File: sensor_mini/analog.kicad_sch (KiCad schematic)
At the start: 7 parts, among them J3 Thermistor_conn, J4 Tank_pressure_conn

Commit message: Clean Up
Removed old files
Cleaned up Schematics
Created new PDFs
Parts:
- renumbered J3 to J2, J4 to J3, R7 to R5, R8 to R6, R9 to R7
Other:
- note added: "Thermistor creates a voltage divider with R7. The resistance is measured using that voltage."
- note added: "Voltage from pin 2 is scaled down with resistor divider and measured."
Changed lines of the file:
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@@
     (stroke (width 0) (type default) (color 0 0 0 0))
+  )
+  (text "Thermistor creates a voltage divider with R7.\nThe resistance is measured using that voltage."
+    (at 171.45 72.39 0)
+    (effects (font (size 1.27 1.27)) (justify left bottom))
+  )
+  (text "Voltage from pin 2 is scaled down with\nresistor divider and measured."
+    (at 172.72 114.3 0)
+    (effects (font (size 1.27 1.27)) (justify left bottom))
   )
   (hierarchical_label "THERM_0" (shape input) (at 132.08 88.9 180)
@@
   (symbol (lib_id "sensors-rescue:Conn_01x03_Female-Connector") (at 165.1 124.46 0) (unit 1)
     (in_bom yes) (on_board yes)
-    (property "Reference" "J4" (id 0) (at 165.8112 123.7996 0)
+    (property "Reference" "J3" (id 0) (at 165.8112 123.7996 0)
       (effects (font (size 1.27 1.27)) (justify left))
     )
@@
     (pin "3")
   )
-  (symbol (lib_id "sensors-rescue:Conn_01x02_Female-Connector") (at 165.1 88.9 0)
+  (symbol (lib_id "sensors-rescue:Conn_01x02_Female-Connector") (at 165.1 88.9 0) (unit 1)
     (in_bom yes) (on_board yes)
-    (property "Reference" "J3" (id 0) (at 165.7858 89.5096 0)
+    (property "Reference" "J2" (id 0) (at 165.7858 89.5096 0)
       (effects (font (size 1.27 1.27)) (justify left))
     )
@@
   (symbol (lib_id "Device:R") (at 154.94 81.28 0) (unit 1)
     (in_bom yes) (on_board yes)
-    (property "Reference" "R9" (id 0) (at 156.718 80.1116 0)
+    (property "Reference" "R7" (id 0) (at 156.718 80.1116 0)
       (effects (font (size 1.27 1.27)) (justify left))
     )
@@
   (symbol (lib_id "power:+15V") (at 154.94 119.38 0) (unit 1)
     (in_bom yes) (on_board yes)
-    (property "Reference" "#PWR058" (id 0) (at 154.94 123.19 0)
+    (property "Reference" "#PWR039" (id 0) (at 154.94 123.19 0)
       (effects (font (size 1.27 1.27)) hide)
     )
@@
   (symbol (lib_id "power:GND") (at 154.94 129.54 0) (unit 1)
     (in_bom yes) (on_board yes)
-    (property "Reference" "#PWR059" (id 0) (at 154.94 135.89 0)
+    (property "Reference" "#PWR040" (id 0) (at 154.94 135.89 0)
       (effects (font (size 1.27 1.27)) hide)
     )
@@
   (symbol (lib_id "power:GND") (at 154.94 93.98 0) (unit 1)
     (in_bom yes) (on_board yes)
-    (property "Reference" "#PWR057" (id 0) (at 154.94 100.33 0)
+    (property "Reference" "#PWR038" (id 0) (at 154.94 100.33 0)
       (effects (font (size 1.27 1.27)) hide)
     )
@@
   (symbol (lib_id "Device:R") (at 142.24 128.27 0) (unit 1)
     (in_bom yes) (on_board yes)
-    (property "Reference" "R7" (id 0) (at 144.018 127.1016 0)
+    (property "Reference" "R5" (id 0) (at 144.018 127.1016 0)
       (effects (font (size 1.27 1.27)) (justify left))
     )
@@
   (symbol (lib_id "Device:R") (at 142.24 139.7 0) (unit 1)
     (in_bom yes) (on_board yes)
-    (property "Reference" "R8" (id 0) (at 144.018 138.5316 0)
+    (property "Reference" "R6" (id 0) (at 144.018 138.5316 0)
       (effects (font (size 1.27 1.27)) (justify left))
     )
@@
   (symbol (lib_id "power:GND") (at 142.24 143.51 0) (unit 1)
     (in_bom yes) (on_board yes)
-    (property "Reference" "#PWR055" (id 0) (at 142.24 149.86 0)
+    (property "Reference" "#PWR036" (id 0) (at 142.24 149.86 0)
       (effects (font (size 1.27 1.27)) hide)
     )
@@
     (pin "1")
   )
-  (symbol (lib_id "power:+3V3") (at 154.94 73.66 0)
+  (symbol (lib_id "power:+3V3") (at 154.94 73.66 0) (unit 1)
     (in_bom yes) (on_board yes)
-    (property "Reference" "#PWR056" (id 0) (at 154.94 77.47 0)
+    (property "Reference" "#PWR037" (id 0) (at 154.94 77.47 0)
       (effects (font (size 1.27 1.27)) hide)
     )

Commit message: ICM-20948
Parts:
- added J? (x3): Thermistor_conn, Connector_JST:JST_PH_S2B-PH-K_1x02_P2.00mm_Horizontal, symbol sensors-rescue:Conn_01x02_Female-Connector
- added R? (x6): R, symbol Device:R
- added R?: R, Resistor_SMD:R_0805_2012Metric_Pad1.15x1.40mm_HandSolder, symbol Device:R
- added TP?: TestPoint, TestPoint:TestPoint_THTPad_2.0x2.0mm_Drill1.0mm, symbol Connector:TestPoint
- added U?: TLV9002IDR, SOIC127P599X175-8N, symbol TLV9002IDR:TLV9002IDR
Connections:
- net +3V3: now also R?.1
- net GND: now also J?.2 (Pin_2), R?.1, R?.2, U?.4 (V-)
- net THERM_0: now also J?.1 (Pin_1), R?.2, TP?.1
- new net: R?.1, R?.1, R?.2, U?.2
- new net: R?.1, R?.1, R?.2, U?.6
- new net: R?.2, U?.7
- new net: J?.1 (Pin_1), U?.5
- new net: R?.2, U?.1
- new net: J?.2 (Pin_2), U?.3
- new net +3.3V: J?.1 (Pin_1), J?.2 (Pin_2), R?.1, R?.2, U?.8 (V+)
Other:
- note added: "Reference Application Note: https://www.ti.com/lit/an/sboa323a/sboa323a.pdf?ts=1668083218662&ref_url=https%253A%252F%252Fwww.google.com%252F"
- note added: "Wheat Stone Bridge Circuit #2"
- note added: "WheatStone Bridge Circuit #1"
- moved on the sheet: J2, J3, R5, R6, R7, TP5, TP6

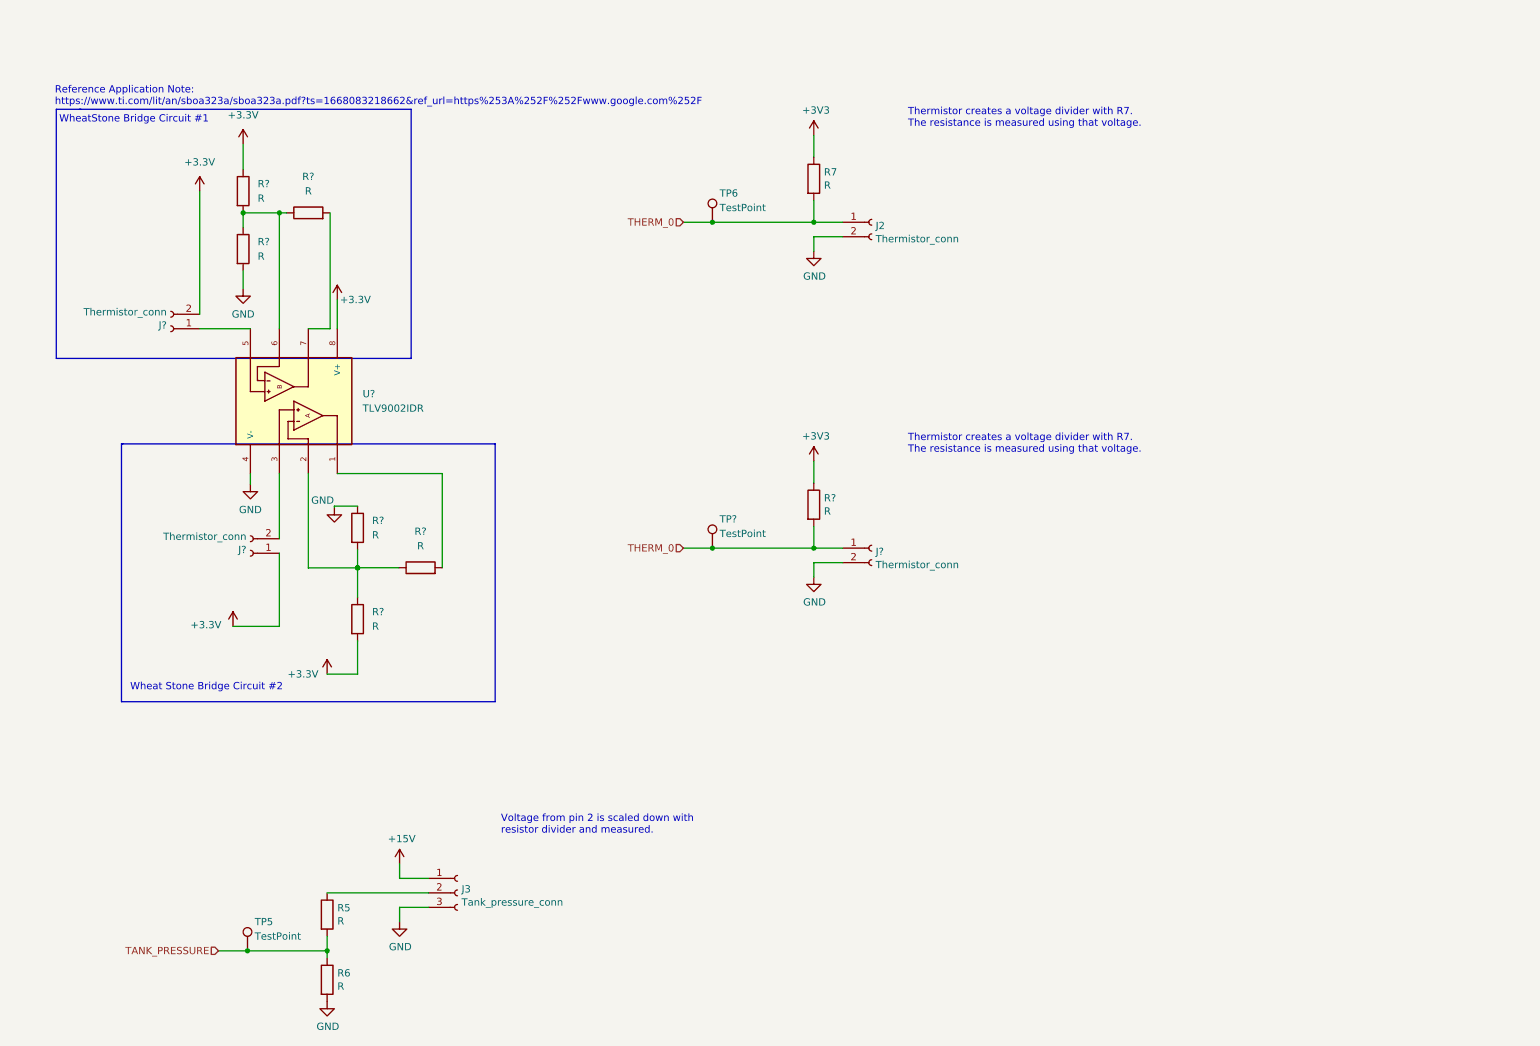
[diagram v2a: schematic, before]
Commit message: Finish Analog Sensors Schematic
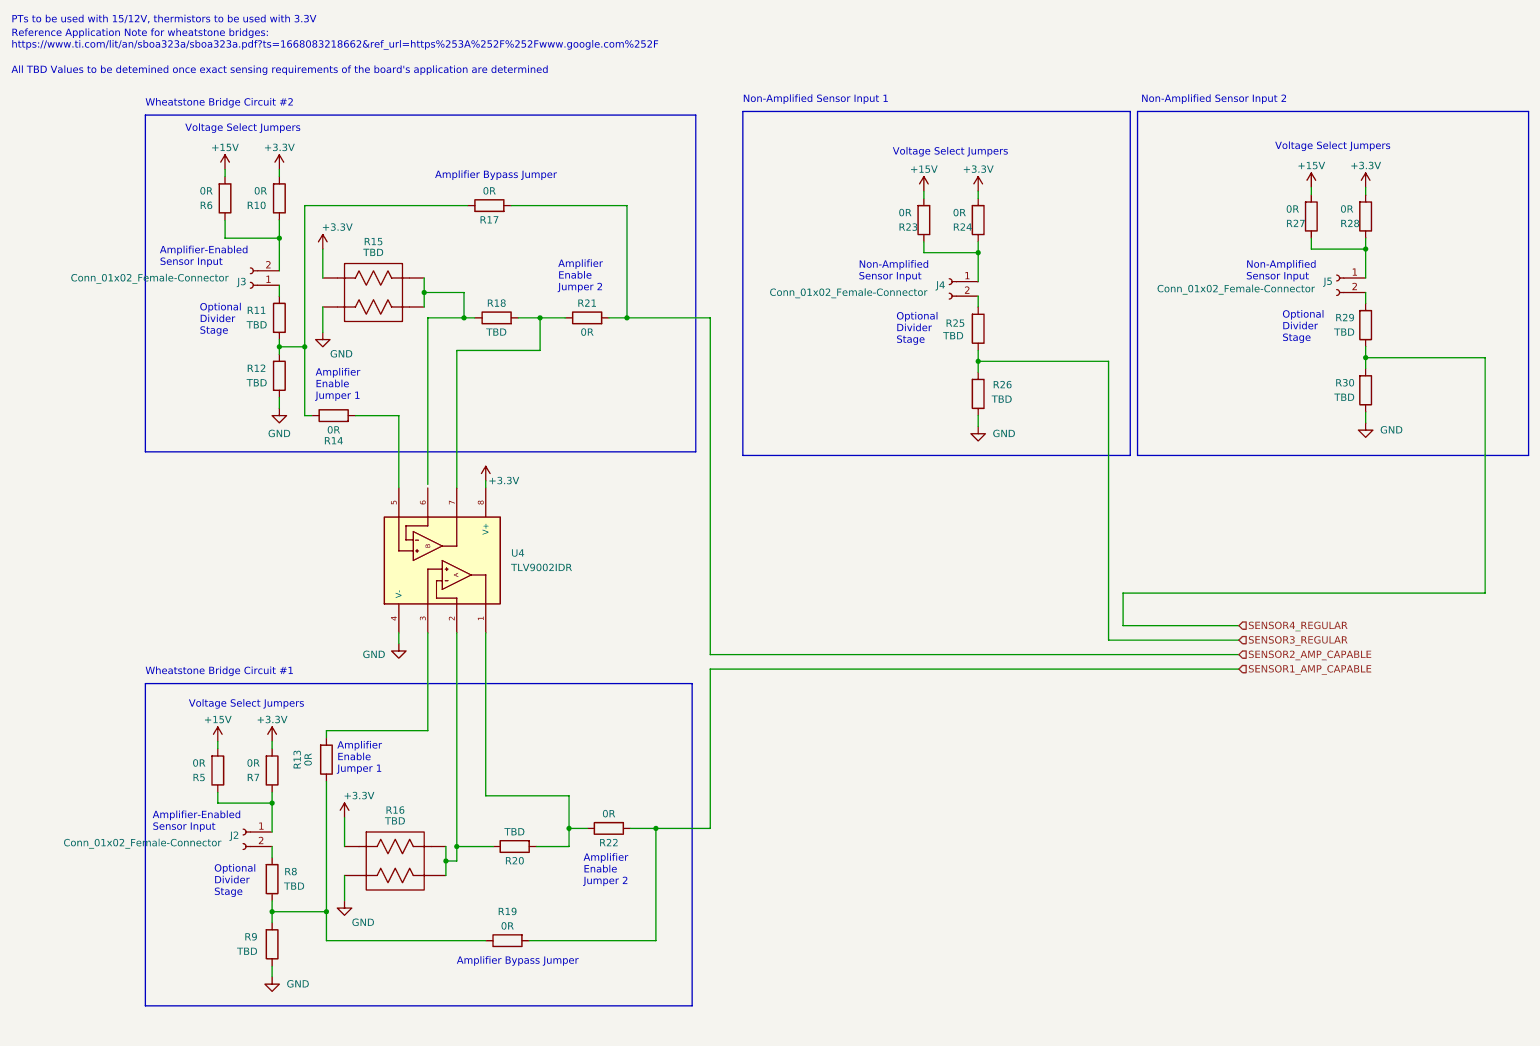
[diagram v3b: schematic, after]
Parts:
- removed J3: Tank_pressure_conn, Connector_JST:JST_PH_S3B-PH-K_1x03_P2.00mm_Horizontal, symbol sensors-rescue:Conn_01x03_Female-Connector
- removed J? (x2): Thermistor_conn, Connector_JST:JST_PH_S2B-PH-K_1x02_P2.00mm_Horizontal, symbol sensors-rescue:Conn_01x02_Female-Connector
- removed R? (x5): R, symbol Device:R
- removed R?: R, Resistor_SMD:R_0805_2012Metric_Pad1.15x1.40mm_HandSolder, symbol Device:R
- removed TP5, TP6, TP?: TestPoint, TestPoint:TestPoint_THTPad_2.0x2.0mm_Drill1.0mm, symbol Connector:TestPoint
- added J4, J5: Conn_01x02_Female-Connector, Connector_JST:JST_PH_S2B-PH-K_1x02_P2.00mm_Horizontal, symbol sensors-rescue:Conn_01x02_Female-Connector
- added R10, R13, R14, R17, R19, R21, R22, R23, R24, R27, R28: 0R, symbol Device:R
- added R11, R12, R20, R25, R26, R29, R30, R8, R9: TBD, symbol Device:R
- added R15, R16: TBD, symbol ACA_Percision_Vishay:2_RES_ARRAY
- J2: value Thermistor_conn -> Conn_01x02_Female-Connector
- J3: renamed from J?; value Thermistor_conn -> Conn_01x02_Female-Connector
- R18: renamed from R?; value R -> TBD
- R5, R6, R7: value R -> 0R; footprint Resistor_SMD:R_0805_2012Metric_Pad1.15x1.40mm_HandSolder -> (none)
- gave numbers to parts that had none: 1
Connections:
- net +15V: now also R5.2, R6.2, R23.2, R27.2
- net +3V3: now also R7.2, U4.8 (V+), R10.2, R15., R16., R24.2, R28.2; no longer R7.1
- net GND: now also R12.2, R15., R16., R26.1, R30.1, R9.1; no longer J2.2 (Pin_2), R6.2
- net at R5.1: now also J2.1 (Pin_1), R7.1
- net at U4.2: now also R16., R20.1
- net at R18.1: now also R15.; no longer U4.6
- net at R18.2, U4.7: now also R21.1
- net at J3.1 (Pin_1): now also R11.1; no longer U4.5
- net at U4.1: now also R20.2, R22.1
- net at U4.3: now also R13.2
- net +3.3V: no longer names the net of J3.2 (Pin_2)
- net +3.3V: now also R6.1, R10.1; no longer U4.8 (V+)
- removed net TANK_PRESSURE: R5.2, R6.1
- removed net THERM_0: J2.1 (Pin_1), R7.2
- new net: J5.1 (Pin_1), R27.1, R28.1
- new net: J5.2 (Pin_2), R29.2
- new net: R13.1, R19.1, R8.1, R9.2
- new net: J4.1 (Pin_1), R23.1, R24.1
- new net: J4.2 (Pin_2), R25.2
- new net: R11.2, R12.1, R14.1, R17.1
- new net: R14.2, U4.5
- new net: J2.2 (Pin_2), R8.2
- new net SENSOR1_AMP_CAPABLE: R19.2, R22.2
- new net SENSOR2_AMP_CAPABLE: R17.2, R21.2
- new net SENSOR3_REGULAR: R25.1, R26.2
- new net SENSOR4_REGULAR: R29.1, R30.2
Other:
- note added: "All TBD Values to be detemined once exact sensing requirements of the board's application are determined"
- note added: "Amplifier Bypass Jumper"
- note added: "Amplifier Enable Jumper 1"
- note added: "Amplifier Enable Jumper 2"
- note added: "Amplifier-Enabled Sensor Input"
- note added: "Non-Amplified Sensor Input"
- note added: "Non-Amplified Sensor Input 1"
- note added: "Non-Amplified Sensor Input 2"
- note added: "Optional Divider Stage"
- note added: "PTs to be used with 15/12V, thermistors to be used with 3.3V"
- note added: "Reference Application Note for wheatstone bridges: https://www.ti.com/lit/an/sboa323a/sboa323a.pdf?ts=1668083218662&ref_url=https%253A%252F%252Fwww.google.com%252F"
- note added: "Voltage Select Jumpers"
- note added: "Wheatstone Bridge Circuit #1"
- note added: "Wheatstone Bridge Circuit #2"
- note removed: "Reference Application Note: https://www.ti.com/lit/an/sboa323a/sboa323a.pdf?ts=1668083218662&ref_url=https%253A%252F%252Fwww.google.com%252F"
- note removed: "Thermistor creates a voltage divider with R7. The resistance is measured using that voltage."
- note removed: "Voltage from pin 2 is scaled down with resistor divider and measured."
- note removed: "Wheat Stone Bridge Circuit #2"
- note removed: "WheatStone Bridge Circuit #1"
- moved on the sheet: J3, R18, U4

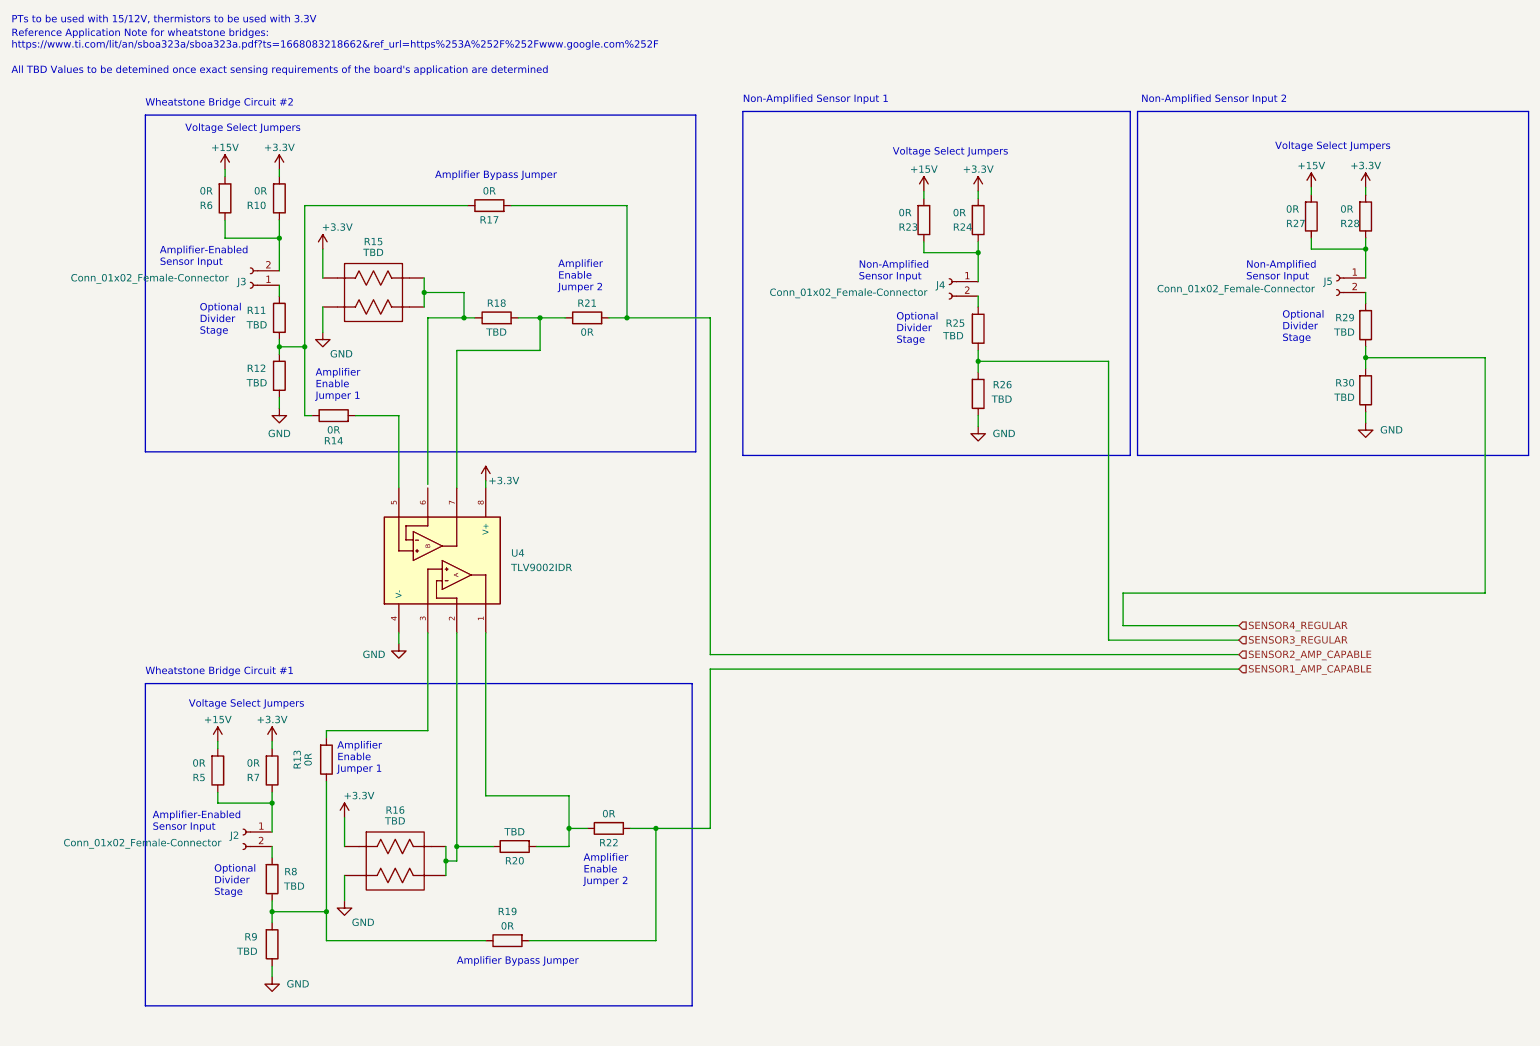
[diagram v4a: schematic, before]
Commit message: Added Test Points For the People
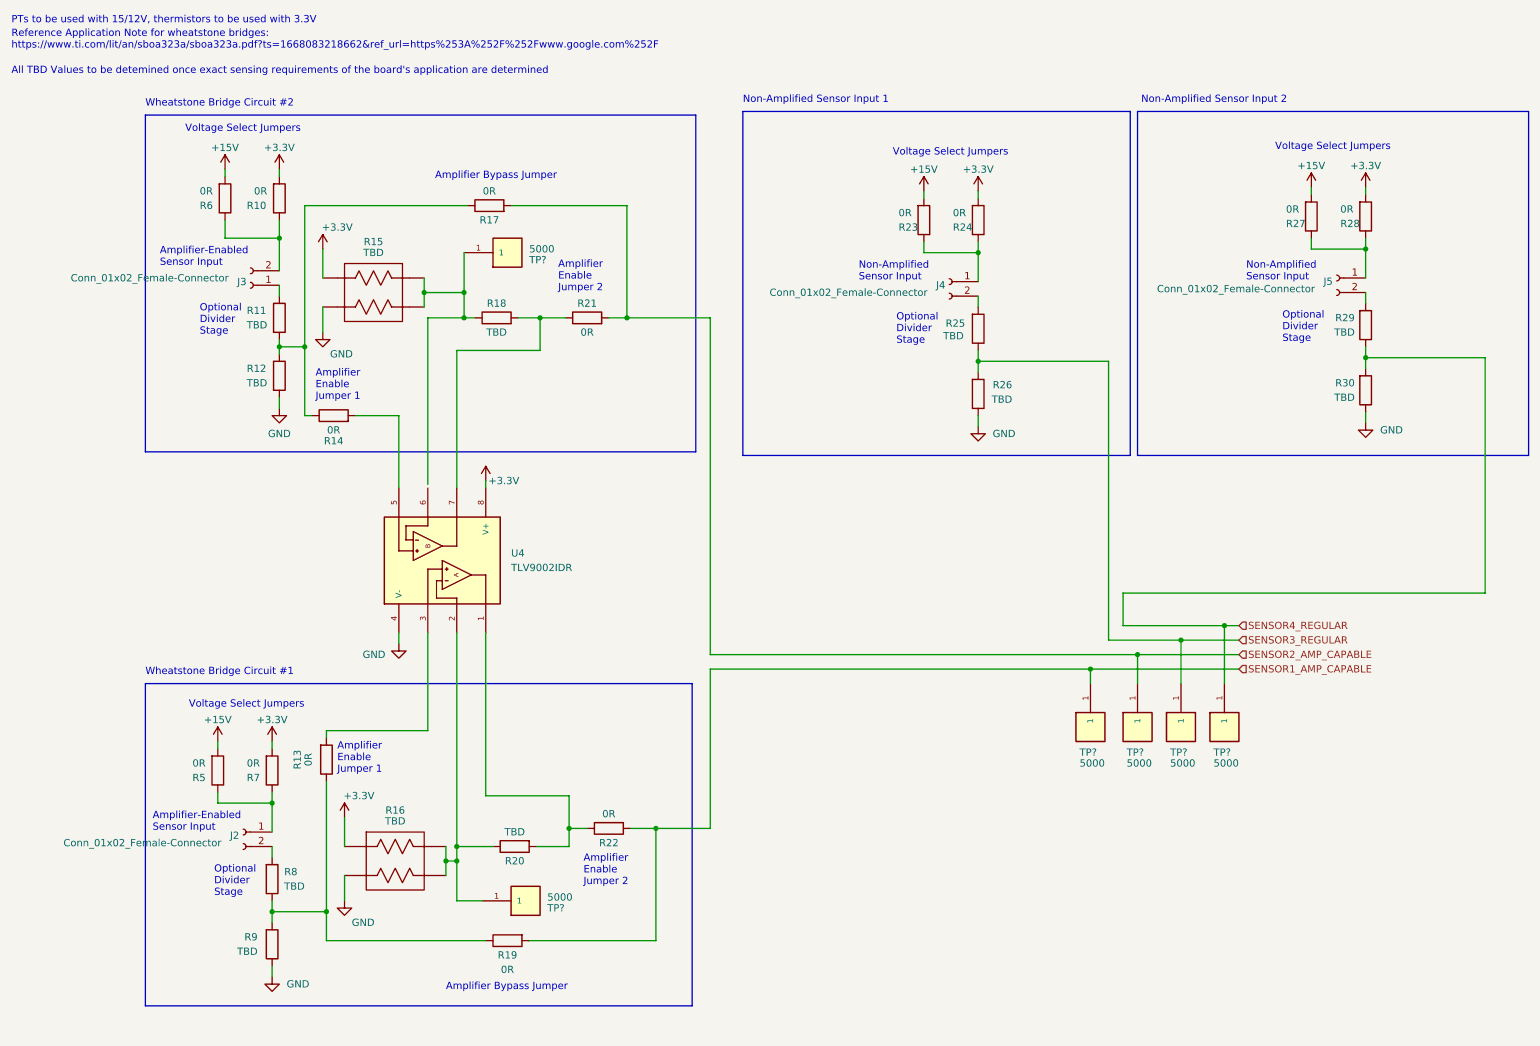
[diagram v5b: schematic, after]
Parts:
- added TP? (x6): 5000, KEYSTONE_5000, symbol Keysight_5000_testpoints:5000
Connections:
- net SENSOR1_AMP_CAPABLE: now also TP?.1
- net SENSOR2_AMP_CAPABLE: now also TP?.1
- net SENSOR3_REGULAR: now also TP?.1
- net SENSOR4_REGULAR: now also TP?.1
- net at R15., R18.1: now also TP?.1
- net at R16., R20.1, U4.2: now also TP?.1
